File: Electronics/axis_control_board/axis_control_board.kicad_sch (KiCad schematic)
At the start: 29 parts, among them Q1 S8050, U2 NRF24L01_Breakout, U3 AMS1117-3.3, U4 LM7805_TO220

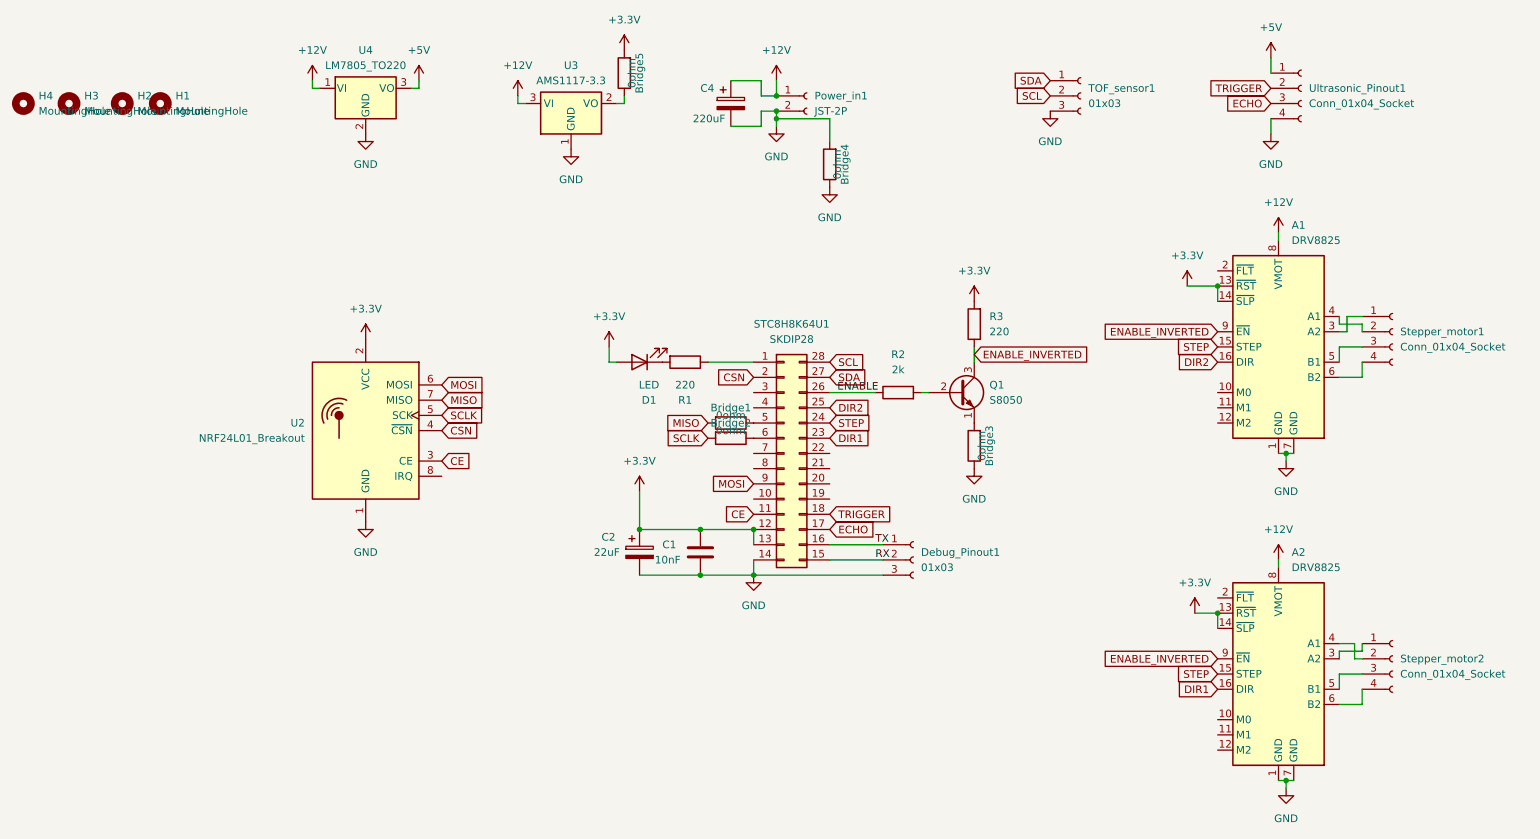
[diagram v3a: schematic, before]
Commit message: finished sensor board PCB
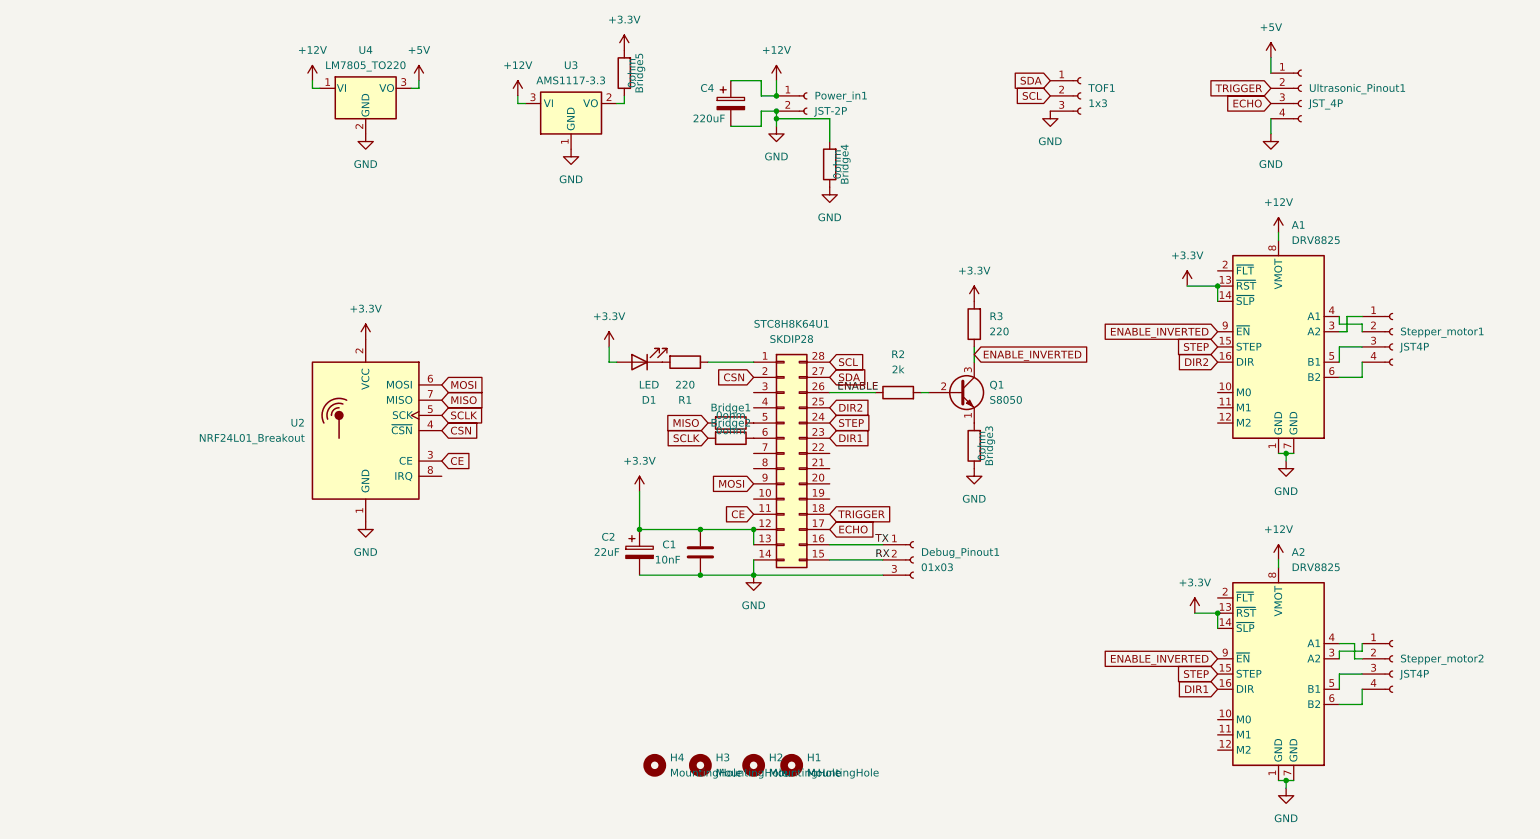
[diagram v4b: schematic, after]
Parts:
- Stepper_motor1, Stepper_motor2: value Conn_01x04_Socket -> JST4P
- TOF1: renamed from TOF_sensor1; value 01x03 -> 1x3
- Ultrasonic_Pinout1: value Conn_01x04_Socket -> JST_4P
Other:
- moved on the sheet: H1, H2, H3, H4
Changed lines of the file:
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@@
     )
   )
-  (symbol (lib_id "Mechanical:MountingHole") (at 38.1 27.94 0) (unit 1)
-    (in_bom yes) (on_board yes) (dnp no) (fields_autoplaced)
-    (property "Reference" "H2" (at 40.64 26.67 0)
-      (effects (font (size 1.27 1.27)) (justify left))
-    )
-    (property "Value" "MountingHole" (at 40.64 29.21 0)
-      (effects (font (size 1.27 1.27)) (justify left))
-    )
-    (property "Footprint" "MountingHole:MountingHole_3.2mm_M3_Pad_TopOnly" (at 38.1 27.94 0)
-      (effects (font (size 1.27 1.27)) hide)
-    )
-    (property "Datasheet" "~" (at 38.1 27.94 0)
+  (symbol (lib_id "Mechanical:MountingHole") (at 143.51 138.43 0) (unit 1)
+    (in_bom yes) (on_board yes) (dnp no) (fields_autoplaced)
+    (property "Reference" "H2" (at 146.05 137.16 0)
+      (effects (font (size 1.27 1.27)) (justify left))
+    )
+    (property "Value" "MountingHole" (at 146.05 139.7 0)
+      (effects (font (size 1.27 1.27)) (justify left))
+    )
+    (property "Footprint" "MountingHole:MountingHole_3.2mm_M3_Pad_TopOnly" (at 143.51 138.43 0)
+      (effects (font (size 1.27 1.27)) hide)
+    )
+    (property "Datasheet" "~" (at 143.51 138.43 0)
       (effects (font (size 1.27 1.27)) hide)
     )
@@
   (symbol (lib_id "Connector:Conn_01x03_Socket") (at 198.12 26.67 0) (unit 1)
     (in_bom yes) (on_board yes) (dnp no) (fields_autoplaced)
-    (property "Reference" "TOF_sensor1" (at 199.39 25.4 0)
-      (effects (font (size 1.27 1.27)) (justify left))
-    )
-    (property "Value" "01x03" (at 199.39 27.94 0)
+    (property "Reference" "TOF1" (at 199.39 25.4 0)
+      (effects (font (size 1.27 1.27)) (justify left))
+    )
+    (property "Value" "1x3" (at 199.39 27.94 0)
       (effects (font (size 1.27 1.27)) (justify left))
     )
@@
       (project "axis_control_board"
         (path "/c464bac3-01d0-4f14-8423-fe4a2abbcdb1"
-          (reference "TOF_sensor1") (unit 1)
+          (reference "TOF1") (unit 1)
         )
       )
@@
       (effects (font (size 1.27 1.27)) (justify left))
     )
-    (property "Value" "Conn_01x04_Socket" (at 251.46 123.19 0)
+    (property "Value" "JST4P" (at 251.46 123.19 0)
       (effects (font (size 1.27 1.27)) (justify left))
     )
@@
     )
   )
-  (symbol (lib_id "Mechanical:MountingHole") (at 44.45 27.94 0) (unit 1)
-    (in_bom yes) (on_board yes) (dnp no) (fields_autoplaced)
-    (property "Reference" "H1" (at 46.99 26.67 0)
-      (effects (font (size 1.27 1.27)) (justify left))
-    )
-    (property "Value" "MountingHole" (at 46.99 29.21 0)
-      (effects (font (size 1.27 1.27)) (justify left))
-    )
-    (property "Footprint" "MountingHole:MountingHole_3.2mm_M3_Pad_TopOnly" (at 44.45 27.94 0)
-      (effects (font (size 1.27 1.27)) hide)
-    )
-    (property "Datasheet" "~" (at 44.45 27.94 0)
+  (symbol (lib_id "Mechanical:MountingHole") (at 149.86 138.43 0) (unit 1)
+    (in_bom yes) (on_board yes) (dnp no) (fields_autoplaced)
+    (property "Reference" "H1" (at 152.4 137.16 0)
+      (effects (font (size 1.27 1.27)) (justify left))
+    )
+    (property "Value" "MountingHole" (at 152.4 139.7 0)
+      (effects (font (size 1.27 1.27)) (justify left))
+    )
+    (property "Footprint" "MountingHole:MountingHole_3.2mm_M3_Pad_TopOnly" (at 149.86 138.43 0)
+      (effects (font (size 1.27 1.27)) hide)
+    )
+    (property "Datasheet" "~" (at 149.86 138.43 0)
       (effects (font (size 1.27 1.27)) hide)
     )
@@
       (effects (font (size 1.27 1.27)) (justify left))
     )
-    (property "Value" "Conn_01x04_Socket" (at 236.22 27.94 0)
+    (property "Value" "JST_4P" (at 236.22 27.94 0)
       (effects (font (size 1.27 1.27)) (justify left))
     )
@@
     )
   )
-  (symbol (lib_id "Mechanical:MountingHole") (at 21.59 27.94 0) (unit 1)
-    (in_bom yes) (on_board yes) (dnp no) (fields_autoplaced)
-    (property "Reference" "H4" (at 24.13 26.67 0)
-      (effects (font (size 1.27 1.27)) (justify left))
-    )
-    (property "Value" "MountingHole" (at 24.13 29.21 0)
-      (effects (font (size 1.27 1.27)) (justify left))
-    )
-    (property "Footprint" "MountingHole:MountingHole_3.2mm_M3_Pad_TopOnly" (at 21.59 27.94 0)
-      (effects (font (size 1.27 1.27)) hide)
-    )
-    (property "Datasheet" "~" (at 21.59 27.94 0)
+  (symbol (lib_id "Mechanical:MountingHole") (at 127 138.43 0) (unit 1)
+    (in_bom yes) (on_board yes) (dnp no) (fields_autoplaced)
+    (property "Reference" "H4" (at 129.54 137.16 0)
+      (effects (font (size 1.27 1.27)) (justify left))
+    )
+    (property "Value" "MountingHole" (at 129.54 139.7 0)
+      (effects (font (size 1.27 1.27)) (justify left))
+    )
+    (property "Footprint" "MountingHole:MountingHole_3.2mm_M3_Pad_TopOnly" (at 127 138.43 0)
+      (effects (font (size 1.27 1.27)) hide)
+    )
+    (property "Datasheet" "~" (at 127 138.43 0)
       (effects (font (size 1.27 1.27)) hide)
     )
@@
       (effects (font (size 1.27 1.27)) (justify left))
     )
-    (property "Value" "Conn_01x04_Socket" (at 251.46 68.58 0)
+    (property "Value" "JST4P" (at 251.46 68.58 0)
       (effects (font (size 1.27 1.27)) (justify left))
     )
@@
     )
   )
-  (symbol (lib_id "Mechanical:MountingHole") (at 29.21 27.94 0) (unit 1)
-    (in_bom yes) (on_board yes) (dnp no) (fields_autoplaced)
-    (property "Reference" "H3" (at 31.75 26.67 0)
-      (effects (font (size 1.27 1.27)) (justify left))
-    )
-    (property "Value" "MountingHole" (at 31.75 29.21 0)
-      (effects (font (size 1.27 1.27)) (justify left))
-    )
-    (property "Footprint" "MountingHole:MountingHole_3.2mm_M3_Pad_TopOnly" (at 29.21 27.94 0)
-      (effects (font (size 1.27 1.27)) hide)
-    )
-    (property "Datasheet" "~" (at 29.21 27.94 0)
-      (effects (font (size 1.27 1.27)) hide)
-    )
+  (symbol (lib_id "Mechanical:MountingHole") (at 134.62 138.43 0) (unit 1)
+    (in_bom yes) (on_board yes) (dnp no) (fields_autoplaced)
+    (property "Reference" "H3" (at 137.16 137.16 0)
+      (effects (font (size 1.27 1.27)) (justify left))
+    )
+    (property "Value" "MountingHole" (at 137.16 139.7 0)
+      (effects (font (size 1.27 1.27)) (justify left))
+    )
+    (property "Footprint" "MountingHole:MountingHole_3.2mm_M3_Pad_TopOnly" (at 134.62 138.43 0)
+      (effects (font (size 1.27 1.27)) hide)
+    )
+    (property "Datasheet" "~" (at 134.62 138.43 0)
+      (effects (font (size 1.27 1.27)) hide)
+    )
